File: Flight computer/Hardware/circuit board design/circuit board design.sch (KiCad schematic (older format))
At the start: 0 parts

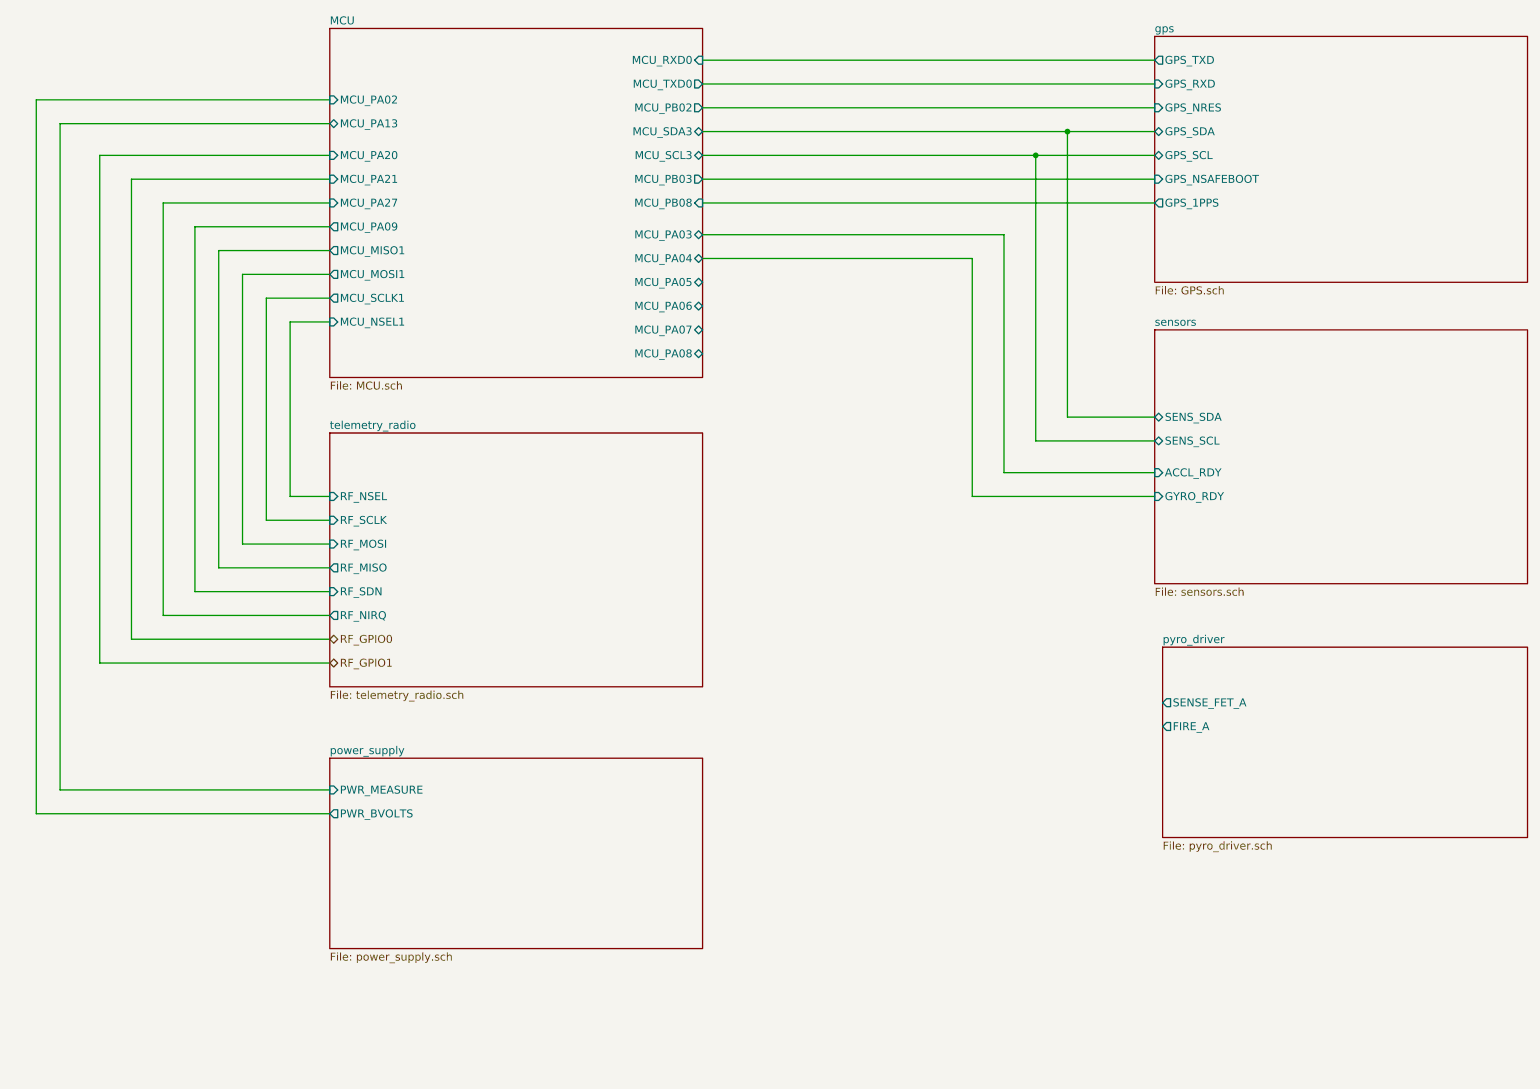
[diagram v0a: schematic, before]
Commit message: created net list for first time
-changed SAML21 to J variant7
-filled in foot prints for all components exept comparator
-changed the footprints of ICSS pico tracker to a local copy
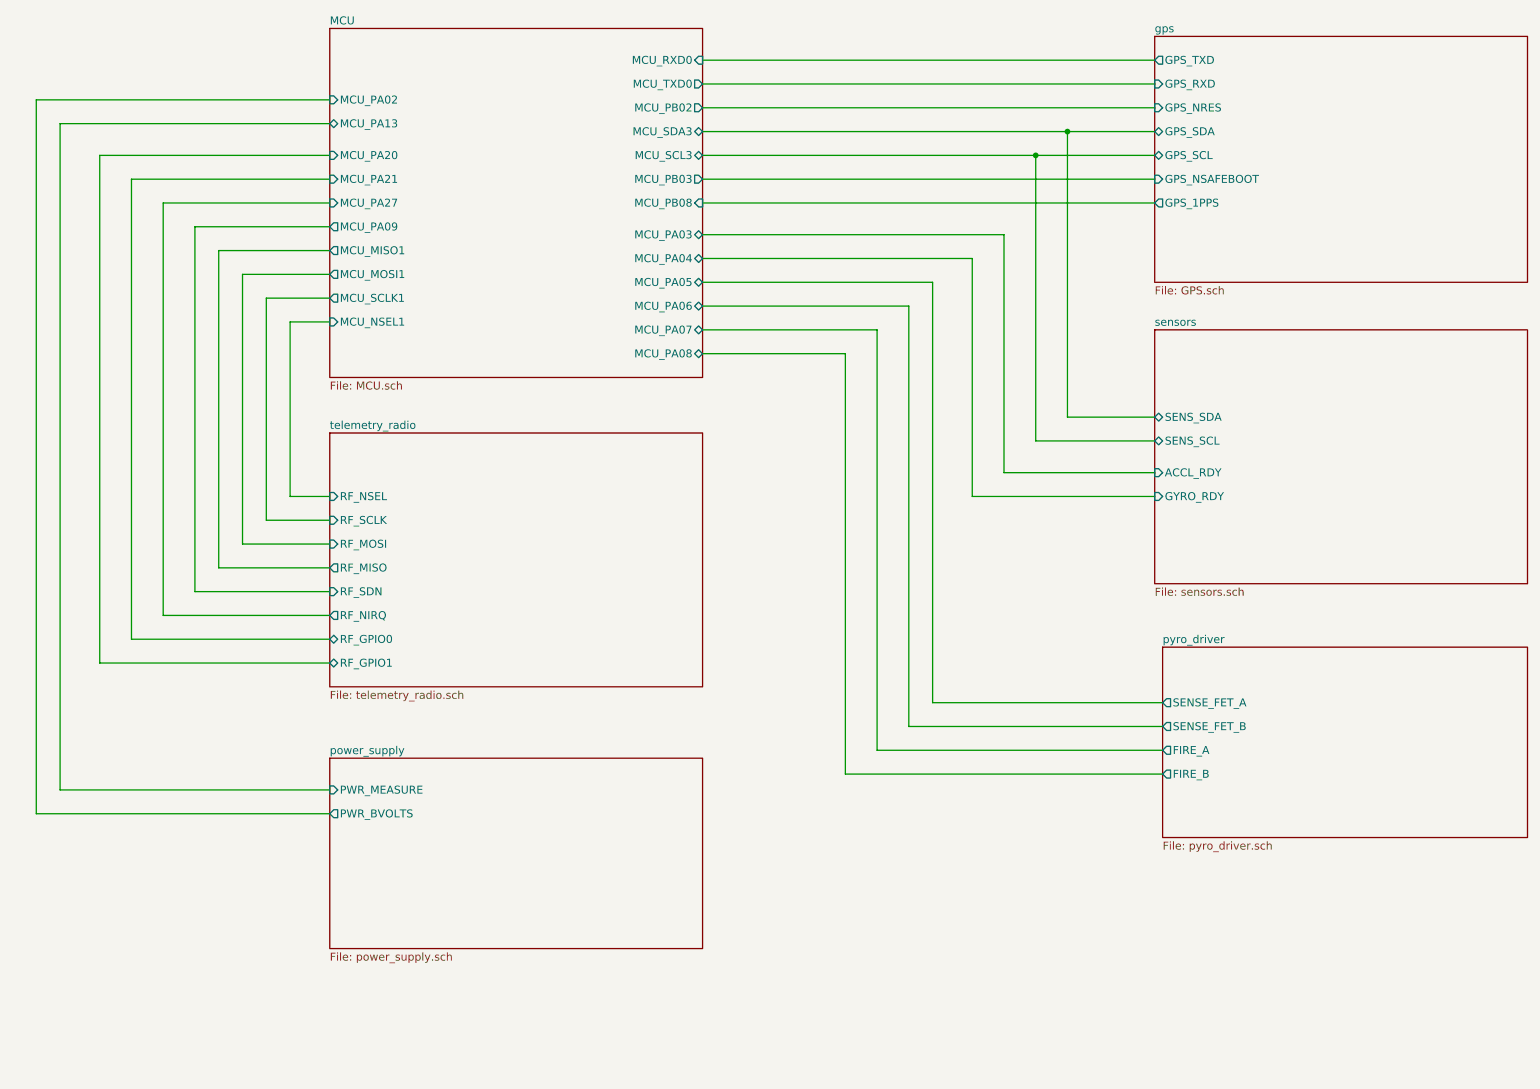
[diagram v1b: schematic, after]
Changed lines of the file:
@@
 F1 "pyro_driver.sch" 50
 F2 "SENSE_FET_A" O L 7950 5350 50
-F3 "FIRE_A" O L 7950 5500 50
+F3 "FIRE_A" O L 7950 5650 50
+F4 "SENSE_FET_B" O L 7950 5500 50
+F5 "FIRE_B" O L 7950 5800 50
 $EndSheet
 Wire Wire Line
@@
 F6 "RF_SDN" I L 2700 4650 50
 F7 "RF_NIRQ" O L 2700 4800 50
+F8 "RF_GPIO0" B L 2700 4950 50
+F9 "RF_GPIO1" B L 2700 5100 50
 $EndSheet
-Text HLabel 2700 4950 2    50   BiDi ~ 0
-RF_GPIO0
-Text HLabel 2700 5100 2    50   BiDi ~ 0
-RF_GPIO1
 Wire Wire Line
 	2700 4800 1650 4800
@@
 Wire Wire Line
 	6750 2550 5050 2550
+Wire Wire Line
+	5050 2700 6500 2700
+Wire Wire Line
+	6500 2700 6500 5350
+Wire Wire Line
+	6500 5350 7950 5350
+Wire Wire Line
+	5050 2850 6350 2850
+Wire Wire Line
+	6350 2850 6350 5500
+Wire Wire Line
+	6350 5500 7950 5500
+Wire Wire Line
+	7950 5650 6150 5650
+Wire Wire Line
+	6150 5650 6150 3000
+Wire Wire Line
+	6150 3000 5050 3000
+Wire Wire Line
+	5050 3150 5950 3150
+Wire Wire Line
+	5950 3150 5950 5800
+Wire Wire Line
+	5950 5800 7950 5800
 $EndSCHEMATC

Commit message: put in the IIS2MDC magnetometer
-fixed the error  spi connection pins for Flash chip
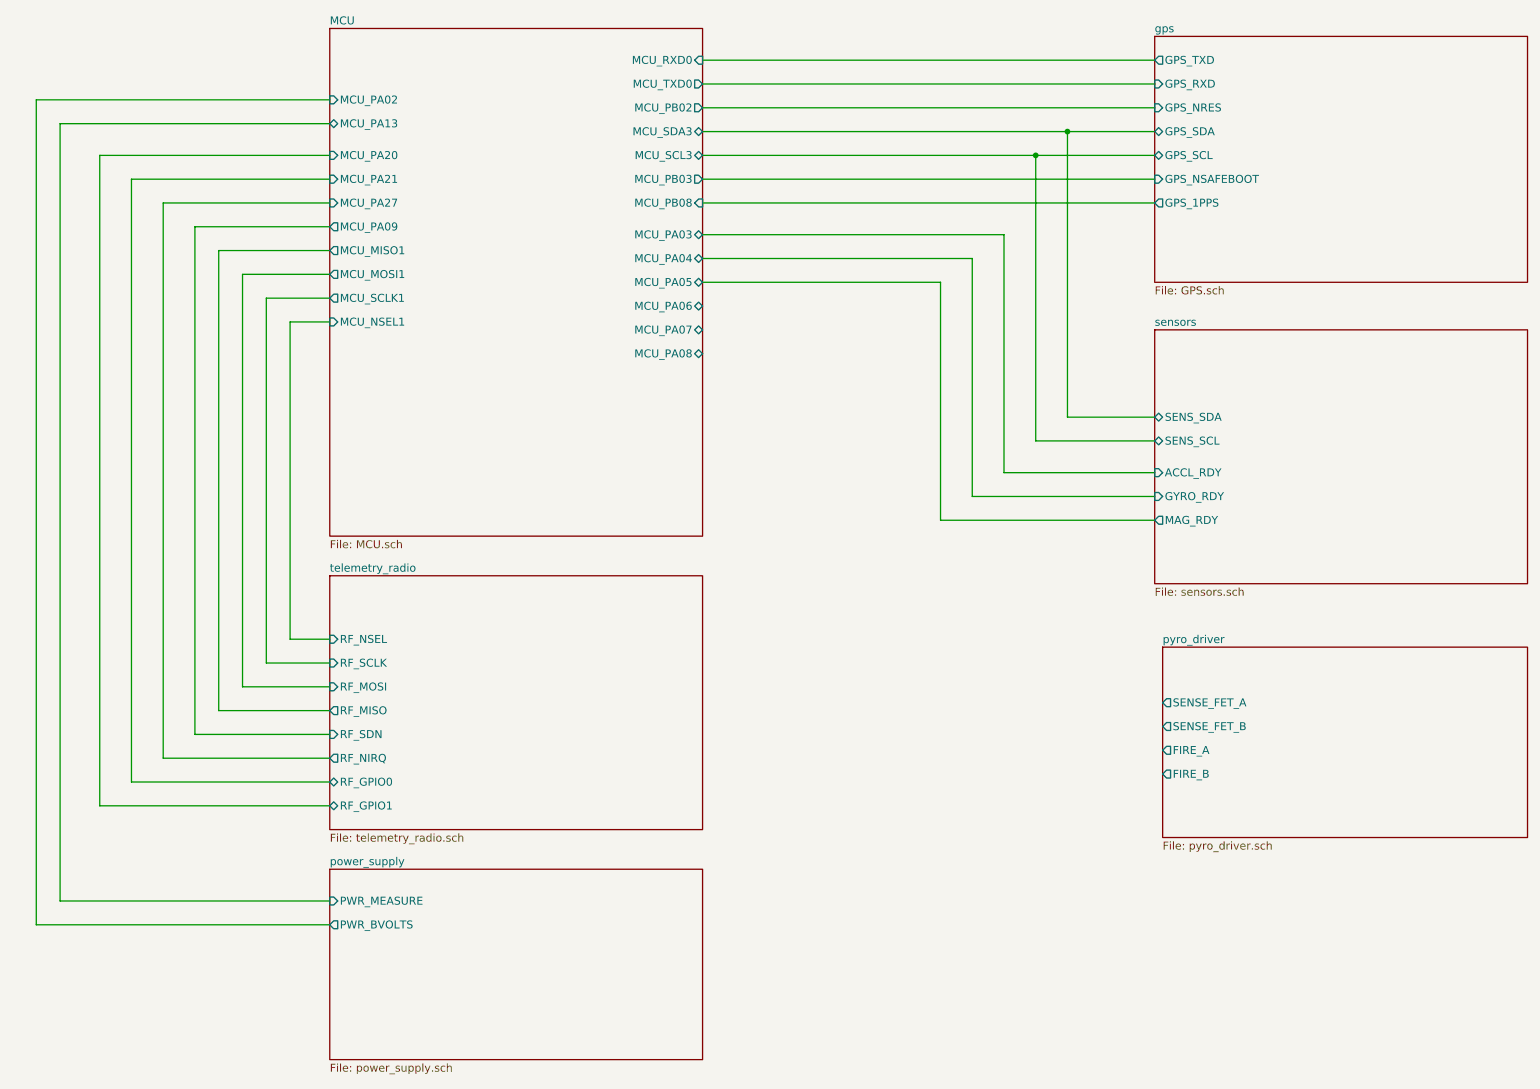
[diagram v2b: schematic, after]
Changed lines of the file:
@@
 F4 "ACCL_RDY" I L 7900 3900 50
 F5 "GYRO_RDY" I L 7900 4050 50
-$EndSheet
-$Sheet
-S 2700 5700 2350 1200
-U 5D5B1705
-F0 "power_supply" 50
-F1 "power_supply.sch" 50
-F2 "PWR_BVOLTS" O L 2700 6050 50
-F3 "PWR_MEASURE" I L 2700 5900 50
+F6 "MAG_RDY" O L 7900 4200 50
 $EndSheet
 $Sheet
@@
 	7900 3700 7150 3700
 Wire Wire Line
+	7350 3550 7350 1750
+Connection ~ 7350 1750
+Wire Wire Line
+	7350 1750 7900 1750
+Wire Wire Line
+	7150 3700 7150 1900
+Connection ~ 7150 1900
+Wire Wire Line
+	7150 1900 7900 1900
+$Sheet
+S 7950 5000 2300 1200
+U 5D6468D5
+F0 "pyro_driver" 50
+F1 "pyro_driver.sch" 50
+F2 "SENSE_FET_A" O L 7950 5350 50
+F3 "FIRE_A" O L 7950 5650 50
+F4 "SENSE_FET_B" O L 7950 5500 50
+F5 "FIRE_B" O L 7950 5800 50
+$EndSheet
+Wire Wire Line
+	7900 3900 6950 3900
+Wire Wire Line
+	6950 3900 6950 2400
+$Sheet
+S 2700 6400 2350 1200
+U 5D5B1705
+F0 "power_supply" 50
+F1 "power_supply.sch" 50
+F2 "PWR_BVOLTS" O L 2700 6750 50
+F3 "PWR_MEASURE" I L 2700 6600 50
+$EndSheet
+Wire Wire Line
+	1000 6600 2700 6600
+Wire Wire Line
+	850  6750 2700 6750
+Wire Wire Line
+	1000 1700 1000 6600
+Wire Wire Line
+	850  1550 850  6750
+Wire Wire Line
+	1250 6000 1250 1900
+Wire Wire Line
+	1450 5850 1450 2050
+Wire Wire Line
+	1650 5700 1650 2200
+Wire Wire Line
+	1850 2350 1850 5550
+Wire Wire Line
+	2450 2950 2450 4950
+Wire Wire Line
+	2000 5400 2000 2500
+Wire Wire Line
+	2150 5250 2150 2650
+Wire Wire Line
+	2300 5100 2300 2800
+Wire Wire Line
+	2700 6000 1250 6000
+Wire Wire Line
+	2700 5850 1450 5850
+Wire Wire Line
+	2700 5700 1650 5700
+Wire Wire Line
+	2700 5550 1850 5550
+Wire Wire Line
+	2450 4950 2700 4950
+Wire Wire Line
+	2700 5250 2150 5250
+Wire Wire Line
+	2700 5400 2000 5400
+Wire Wire Line
+	2700 5100 2300 5100
+$Sheet
+S 2700 4550 2350 1600
+U 5D5B17D8
+F0 "telemetry_radio" 50
+F1 "telemetry_radio.sch" 50
+F2 "RF_SCLK" I L 2700 5100 50
+F3 "RF_MISO" O L 2700 5400 50
+F4 "RF_MOSI" I L 2700 5250 50
+F5 "RF_NSEL" I L 2700 4950 50
+F6 "RF_SDN" I L 2700 5550 50
+F7 "RF_NIRQ" O L 2700 5700 50
+F8 "RF_GPIO0" B L 2700 5850 50
+F9 "RF_GPIO1" B L 2700 6000 50
+$EndSheet
+Wire Wire Line
+	7900 4050 6750 4050
+Wire Wire Line
+	6750 4050 6750 2550
+Wire Wire Line
+	1650 2200 2700 2200
+Wire Wire Line
+	1450 2050 2700 2050
+Wire Wire Line
+	1250 1900 2700 1900
+Wire Wire Line
+	7900 2200 5050 2200
+Wire Wire Line
+	5050 1600 7900 1600
+Wire Wire Line
+	5050 2050 7900 2050
+Wire Wire Line
+	2700 1700 1000 1700
+Wire Wire Line
+	1850 2350 2700 2350
+Wire Wire Line
+	6750 2550 5050 2550
+Wire Wire Line
+	6950 2400 5050 2400
+Wire Wire Line
+	2700 1550 850  1550
+Wire Wire Line
 	7900 1300 5050 1300
 Wire Wire Line
 	5050 1450 7900 1450
+Wire Wire Line
+	5050 1900 7150 1900
+Wire Wire Line
+	5050 1750 7350 1750
+Wire Wire Line
+	2000 2500 2700 2500
+Wire Wire Line
+	2700 2950 2450 2950
+Wire Wire Line
+	2300 2800 2700 2800
+Wire Wire Line
+	2150 2650 2700 2650
 $Sheet
-S 2700 1100 2350 2200
+S 2700 1100 2350 3200
 U 5D5B15F7
 F0 "MCU" 50
@@
 $EndSheet
 Wire Wire Line
-	5050 1750 7350 1750
+	5050 2700 6550 2700
 Wire Wire Line
-	5050 1900 7150 1900
+	6550 2700 6550 4200
 Wire Wire Line
-	7350 3550 7350 1750
-Connection ~ 7350 1750
-Wire Wire Line
-	7350 1750 7900 1750
-Wire Wire Line
-	7150 3700 7150 1900
-Connection ~ 7150 1900
-Wire Wire Line
-	7150 1900 7900 1900
-Wire Wire Line
-	5050 2050 7900 2050
-Wire Wire Line
-	7900 2200 5050 2200
-Wire Wire Line
-	5050 1600 7900 1600
-$Sheet
-S 7950 5000 2300 1200
-U 5D6468D5
-F0 "pyro_driver" 50
-F1 "pyro_driver.sch" 50
-F2 "SENSE_FET_A" O L 7950 5350 50
-F3 "FIRE_A" O L 7950 5650 50
-F4 "SENSE_FET_B" O L 7950 5500 50
-F5 "FIRE_B" O L 7950 5800 50
-$EndSheet
-Wire Wire Line
-	2700 1550 850  1550
-Wire Wire Line
-	850  1550 850  6050
-Wire Wire Line
-	850  6050 2700 6050
-Wire Wire Line
-	2700 1700 1000 1700
-Wire Wire Line
-	1000 1700 1000 5900
-Wire Wire Line
-	1000 5900 2700 5900
-Wire Wire Line
-	2000 2500 2700 2500
-Wire Wire Line
-	2150 2650 2700 2650
-Wire Wire Line
-	2300 2800 2700 2800
-Wire Wire Line
-	2700 2950 2450 2950
-Wire Wire Line
-	2450 4050 2700 4050
-Wire Wire Line
-	2700 4350 2150 4350
-Wire Wire Line
-	2700 4500 2000 4500
-Wire Wire Line
-	2700 4200 2300 4200
-Wire Wire Line
-	2300 4200 2300 2800
-Wire Wire Line
-	2150 4350 2150 2650
-Wire Wire Line
-	2000 4500 2000 2500
-Wire Wire Line
-	2450 2950 2450 4050
-Wire Wire Line
-	2700 4650 1850 4650
-Wire Wire Line
-	1850 2350 2700 2350
-Wire Wire Line
-	1850 2350 1850 4650
-$Sheet
-S 2700 3650 2350 1600
-U 5D5B17D8
-F0 "telemetry_radio" 50
-F1 "telemetry_radio.sch" 50
-F2 "RF_SCLK" I L 2700 4200 50
-F3 "RF_MISO" O L 2700 4500 50
-F4 "RF_MOSI" I L 2700 4350 50
-F5 "RF_NSEL" I L 2700 4050 50
-F6 "RF_SDN" I L 2700 4650 50
-F7 "RF_NIRQ" O L 2700 4800 50
-F8 "RF_GPIO0" B L 2700 4950 50
-F9 "RF_GPIO1" B L 2700 5100 50
-$EndSheet
-Wire Wire Line
-	2700 4800 1650 4800
-Wire Wire Line
-	1650 4800 1650 2200
-Wire Wire Line
-	1650 2200 2700 2200
-Wire Wire Line
-	2700 4950 1450 4950
-Wire Wire Line
-	1450 4950 1450 2050
-Wire Wire Line
-	1450 2050 2700 2050
-Wire Wire Line
-	2700 5100 1250 5100
-Wire Wire Line
-	1250 5100 1250 1900
-Wire Wire Line
-	1250 1900 2700 1900
-Wire Wire Line
-	7900 3900 6950 3900
-Wire Wire Line
-	6950 3900 6950 2400
-Wire Wire Line
-	6950 2400 5050 2400
-Wire Wire Line
-	7900 4050 6750 4050
-Wire Wire Line
-	6750 4050 6750 2550
-Wire Wire Line
-	6750 2550 5050 2550
-Wire Wire Line
-	5050 2700 6500 2700
-Wire Wire Line
-	6500 2700 6500 5350
-Wire Wire Line
-	6500 5350 7950 5350
-Wire Wire Line
-	5050 2850 6350 2850
-Wire Wire Line
-	6350 2850 6350 5500
-Wire Wire Line
-	6350 5500 7950 5500
-Wire Wire Line
-	7950 5650 6150 5650
-Wire Wire Line
-	6150 5650 6150 3000
-Wire Wire Line
-	6150 3000 5050 3000
-Wire Wire Line
-	5050 3150 5950 3150
-Wire Wire Line
-	5950 3150 5950 5800
-Wire Wire Line
-	5950 5800 7950 5800
+	6550 4200 7900 4200
 $EndSCHEMATC
